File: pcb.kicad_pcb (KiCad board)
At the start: 2 copper layers, 120.7 x 70.6 mm, 11 parts, among them U1 Pico

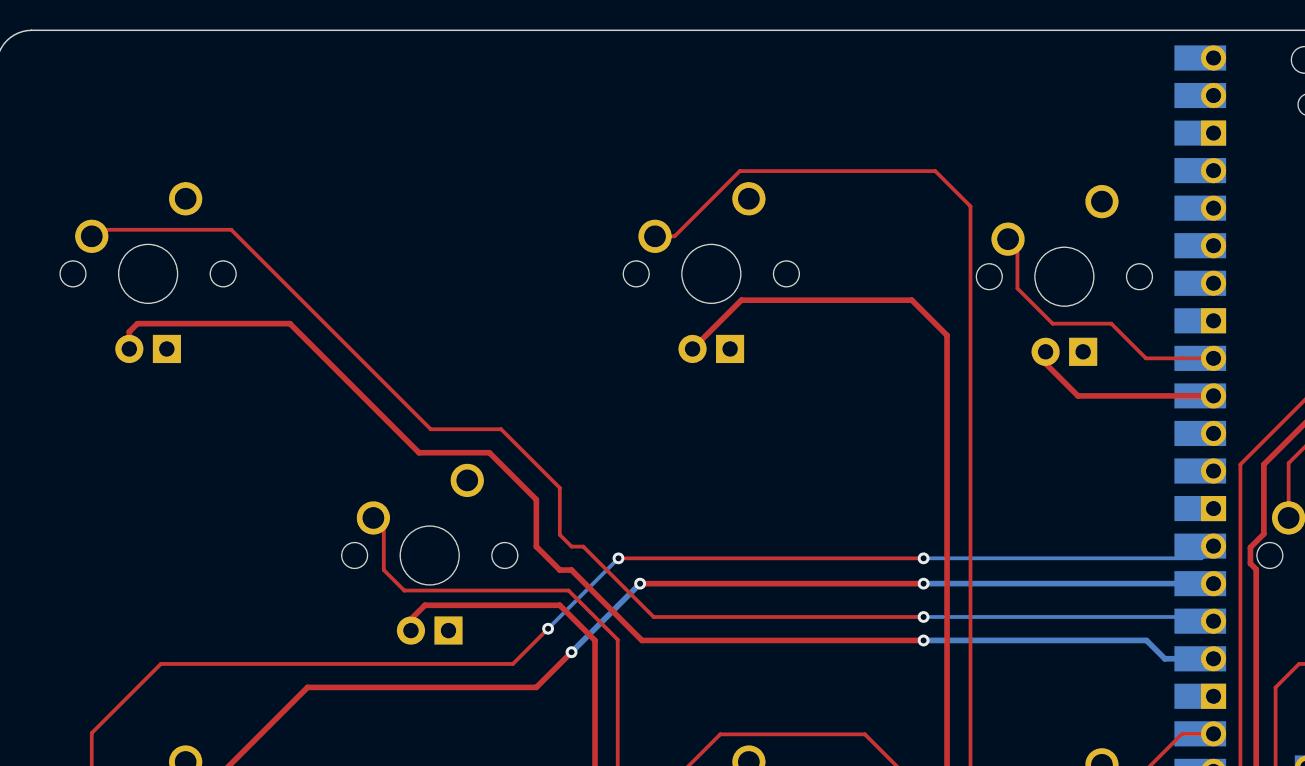
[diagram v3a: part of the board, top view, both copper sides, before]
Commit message: WS2812B strip connector routing
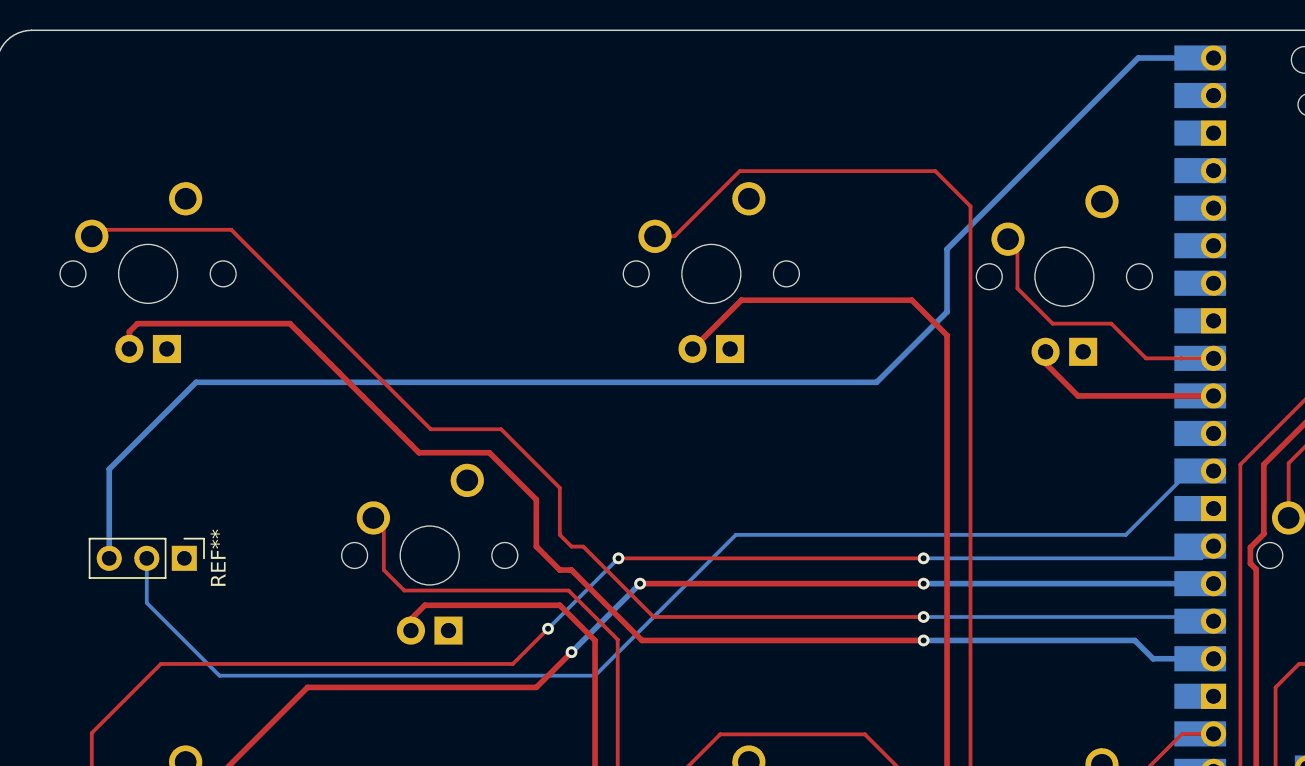
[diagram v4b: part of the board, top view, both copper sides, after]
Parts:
- added REF**: PinHeader_1x03_P2.54mm_Vertical, Connector_PinHeader_2.54mm:PinHeader_1x03_P2.54mm_Vertical, F.Cu at (94.5, 95.2)
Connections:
- U1 pad 29: unconnected-(U1-Pad29) -> DIN
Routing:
- net +5V: track 0.00 -> 94.7 mm
- net DIN: track 0.00 -> 83.0 mm
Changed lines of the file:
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@@
   (net 33 "unconnected-(U1-Pad20)")
   (net 34 "P1 CN")
-  (net 35 "unconnected-(U1-Pad29)")
+  (net 35 "DIN")
   (footprint "MX_Only:MXOnly-1U" (layer "F.Cu")
     (at 192.01775 114.107998)
@@
     (pad "4" thru_hole rect locked (at 1.27 5.08) (size 1.905 1.905) (drill 1.04) (layers *.Cu "B.Mask")
       (net 2 "GND") (pinfunction "LEDGND") (pintype "passive"))
+  )
+  (footprint "Connector_PinHeader_2.54mm:PinHeader_1x03_P2.54mm_Vertical" (layer "F.Cu")
+    (at 94.45625 95.25 -90)
+    (descr "Through hole straight pin header, 1x03, 2.54mm pitch, single row")
+    (tags "Through hole pin header THT 1x03 2.54mm single row")
+    (attr through_hole)
+    (fp_text reference "REF**" (at 0 -2.33 90) (layer "F.SilkS")
+      (effects (font (size 1 1) (thickness 0.15)))
+    )
+    (fp_text value "PinHeader_1x03_P2.54mm_Vertical" (at 0 7.41 90) (layer "F.Fab")
+      (effects (font (size 1 1) (thickness 0.15)))
+    )
+    (fp_text user "${REFERENCE}" (at 0 2.54) (layer "F.Fab")
+      (effects (font (size 1 1) (thickness 0.15)))
+    )
+    (fp_line (start -1.33 6.41) (end 1.33 6.41) (layer "F.SilkS") (width 0.12))
+    (fp_line (start -1.33 1.27) (end -1.33 6.41) (layer "F.SilkS") (width 0.12))
+    (fp_line (start -1.33 -1.33) (end 0 -1.33) (layer "F.SilkS") (width 0.12))
+    (fp_line (start -1.33 1.27) (end 1.33 1.27) (layer "F.SilkS") (width 0.12))
+    (fp_line (start 1.33 1.27) (end 1.33 6.41) (layer "F.SilkS") (width 0.12))
+    (fp_line (start -1.33 0) (end -1.33 -1.33) (layer "F.SilkS") (width 0.12))
+    (fp_line (start 1.8 -1.8) (end -1.8 -1.8) (layer "F.CrtYd") (width 0.05))
+    (fp_line (start -1.8 6.85) (end 1.8 6.85) (layer "F.CrtYd") (width 0.05))
+    (fp_line (start -1.8 -1.8) (end -1.8 6.85) (layer "F.CrtYd") (width 0.05))
+    (fp_line (start 1.8 6.85) (end 1.8 -1.8) (layer "F.CrtYd") (width 0.05))
+    (fp_line (start -1.27 6.35) (end -1.27 -0.635) (layer "F.Fab") (width 0.1))
+    (fp_line (start -0.635 -1.27) (end 1.27 -1.27) (layer "F.Fab") (width 0.1))
+    (fp_line (start -1.27 -0.635) (end -0.635 -1.27) (layer "F.Fab") (width 0.1))
+    (fp_line (start 1.27 -1.27) (end 1.27 6.35) (layer "F.Fab") (width 0.1))
+    (fp_line (start 1.27 6.35) (end -1.27 6.35) (layer "F.Fab") (width 0.1))
+    (pad "1" thru_hole rect (at 0 0 270) (size 1.7 1.7) (drill 1) (layers *.Cu *.Mask)
+      (net 2 "GND"))
+    (pad "2" thru_hole oval (at 0 2.54 270) (size 1.7 1.7) (drill 1) (layers *.Cu *.Mask)
+      (net 35 "DIN"))
+    (pad "3" thru_hole oval (at 0 5.08 270) (size 1.7 1.7) (drill 1) (layers *.Cu *.Mask)
+      (net 1 "+5V"))
+    (model "${KICAD6_3DMODEL_DIR}/Connector_PinHeader_2.54mm.3dshapes/PinHeader_1x03_P2.54mm_Vertical.wrl"
+      (offset (xyz 0 0 0))
+      (scale (xyz 1 1 1))
+      (rotate (xyz 0 0 0))
+    )
   )
   (footprint "MX_Only:MXOnly-1U" (layer "F.Cu")
@@
       (net 2 "GND") (pinfunction "GND") (pintype "power_in"))
     (pad "29" thru_hole oval (at 8.89 -3.81 180) (size 1.7 1.7) (drill 1.02) (layers *.Cu *.Mask)
-      (net 35 "unconnected-(U1-Pad29)") (pinfunction "GPIO22") (pintype "bidirectional"))
+      (net 35 "DIN") (pinfunction "GPIO22") (pintype "bidirectional"))
     (pad "29" smd rect (at 8.89 -3.81 180) (size 3.5 1.7) (drill (offset 0.9 0)) (layers "B.Cu" "B.Mask")
-      (net 35 "unconnected-(U1-Pad29)") (pinfunction "GPIO22") (pintype "bidirectional"))
+      (net 35 "DIN") (pinfunction "GPIO22") (pintype "bidirectional"))
     (pad "30" smd rect (at 8.89 -1.27 180) (size 3.5 1.7) (drill (offset 0.9 0)) (layers "B.Cu" "B.Mask")
       (net 21 "unconnected-(U1-Pad30)") (pinfunction "RUN") (pintype "input"))
@@
   (gr_line (start 202.40625 61.9125) (end 202.40625 127.79375) (layer "Edge.Cuts") (width 0.1))
   (gr_arc (start 202.40625 127.79375) (mid 201.708798 129.477548) (end 200.025 130.175) (layer "Edge.Cuts") (width 0.1))
+  (segment (start 89.37625 89.2175) (end 95.25 83.34375) (width 0.381) (layer "B.Cu") (net 1))
+  (segment (start 158.981632 61.402998) (end 164.07775 61.402998) (width 0.381) (layer "B.Cu") (net 1))
+  (segment (start 95.25 83.34375) (end 141.2875 83.34375) (width 0.381) (layer "B.Cu") (net 1))
+  (segment (start 146.05 78.58125) (end 146.05 74.33463) (width 0.381) (layer "B.Cu") (net 1))
+  (segment (start 141.2875 83.34375) (end 146.05 78.58125) (width 0.381) (layer "B.Cu") (net 1))
+  (segment (start 146.05 74.33463) (end 158.981632 61.402998) (width 0.381) (layer "B.Cu") (net 1))
+  (segment (start 89.37625 95.25) (end 89.37625 89.2175) (width 0.381) (layer "B.Cu") (net 1))
   (segment (start 88.19525 107.06725) (end 88.19525 111.567998) (width 0.254) (layer "F.Cu") (net 3))
   (segment (start 123.825 95.25) (end 144.4625 95.25) (width 0.254) (layer "F.Cu") (net 3))
@@
   (segment (start 110.33125 88.10625) (end 115.09375 88.10625) (width 0.381) (layer "F.Cu") (net 6))
   (via (at 144.4625 100.80625) (size 0.8) (drill 0.4) (layers "F.Cu" "B.Cu") (net 6))
-  (segment (start 159.54375 100.80625) (end 160.780498 102.042998) (width 0.381) (layer "B.Cu") (net 6))
-  (segment (start 160.780498 102.042998) (end 164.07775 102.042998) (width 0.381) (layer "B.Cu") (net 6))
-  (segment (start 144.4625 100.80625) (end 159.54375 100.80625) (width 0.381) (layer "B.Cu") (net 6))
+  (segment (start 159.986748 102.042998) (end 164.07775 102.042998) (width 0.381) (layer "B.Cu") (net 6))
+  (segment (start 158.75 100.80625) (end 159.986748 102.042998) (width 0.381) (layer "B.Cu") (net 6))
+  (segment (start 144.4625 100.80625) (end 158.75 100.80625) (width 0.381) (layer "B.Cu") (net 6))
   (segment (start 109.78525 100.137998) (end 109.78525 99.367875) (width 0.381) (layer "F.Cu") (net 7))
   (segment (start 148.43125 129.38125) (end 162.71875 129.38125) (width 0.381) (layer "F.Cu") (net 7))
@@
   (segment (start 178.59375 98.87309) (end 178.59375 110.33125) (width 0.254) (layer "F.Cu") (net 34))
   (segment (start 171.45 118.26875) (end 161.925 127.79375) (width 0.254) (layer "F.Cu") (net 34))
+  (segment (start 162.46375 89.342998) (end 164.07775 89.342998) (width 0.254) (layer "B.Cu") (net 35))
+  (segment (start 131.7625 93.6625) (end 158.144248 93.6625) (width 0.254) (layer "B.Cu") (net 35))
+  (segment (start 158.144248 93.6625) (end 162.46375 89.342998) (width 0.254) (layer "B.Cu") (net 35))
+  (segment (start 96.8375 103.1875) (end 122.2375 103.1875) (width 0.254) (layer "B.Cu") (net 35))
+  (segment (start 122.2375 103.1875) (end 131.7625 93.6625) (width 0.254) (layer "B.Cu") (net 35))
+  (segment (start 91.91625 98.26625) (end 96.8375 103.1875) (width 0.254) (layer "B.Cu") (net 35))
+  (segment (start 91.91625 95.25) (end 91.91625 98.26625) (width 0.254) (layer "B.Cu") (net 35))
 )

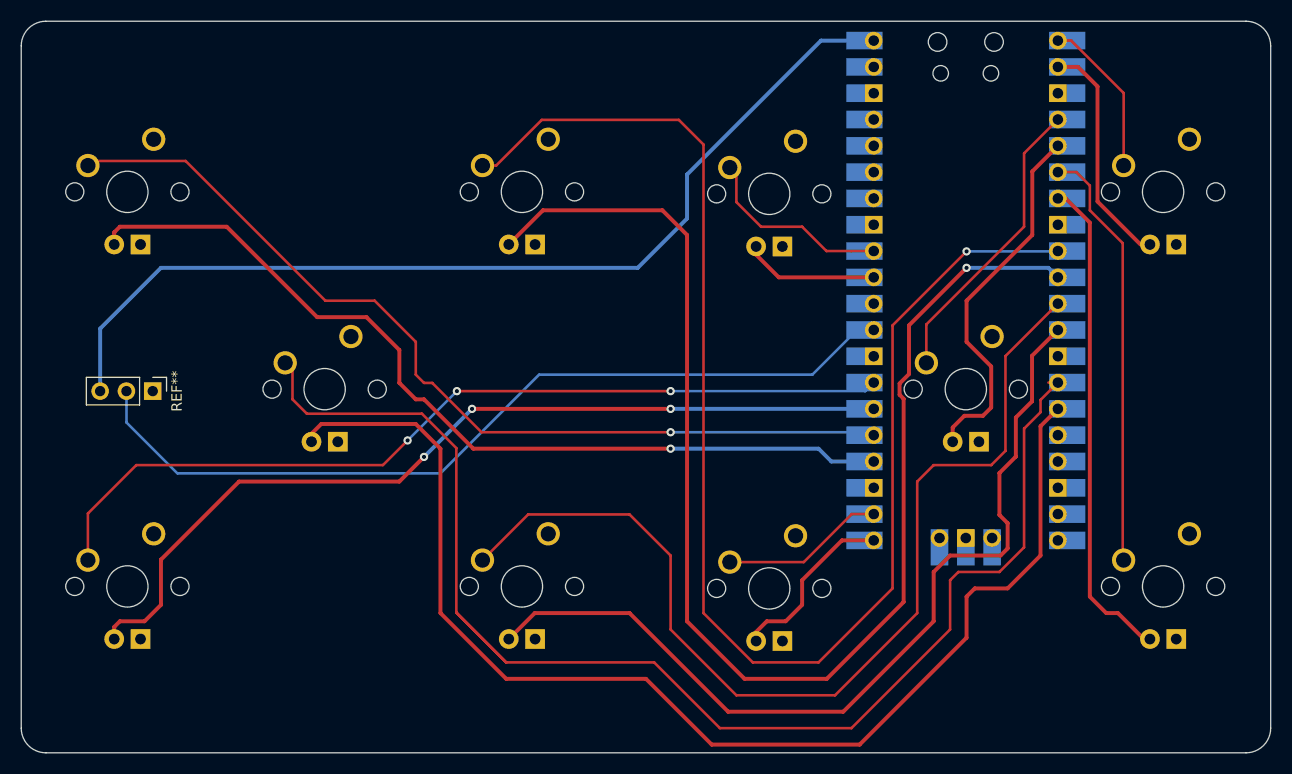
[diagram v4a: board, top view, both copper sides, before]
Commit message: Ground fill
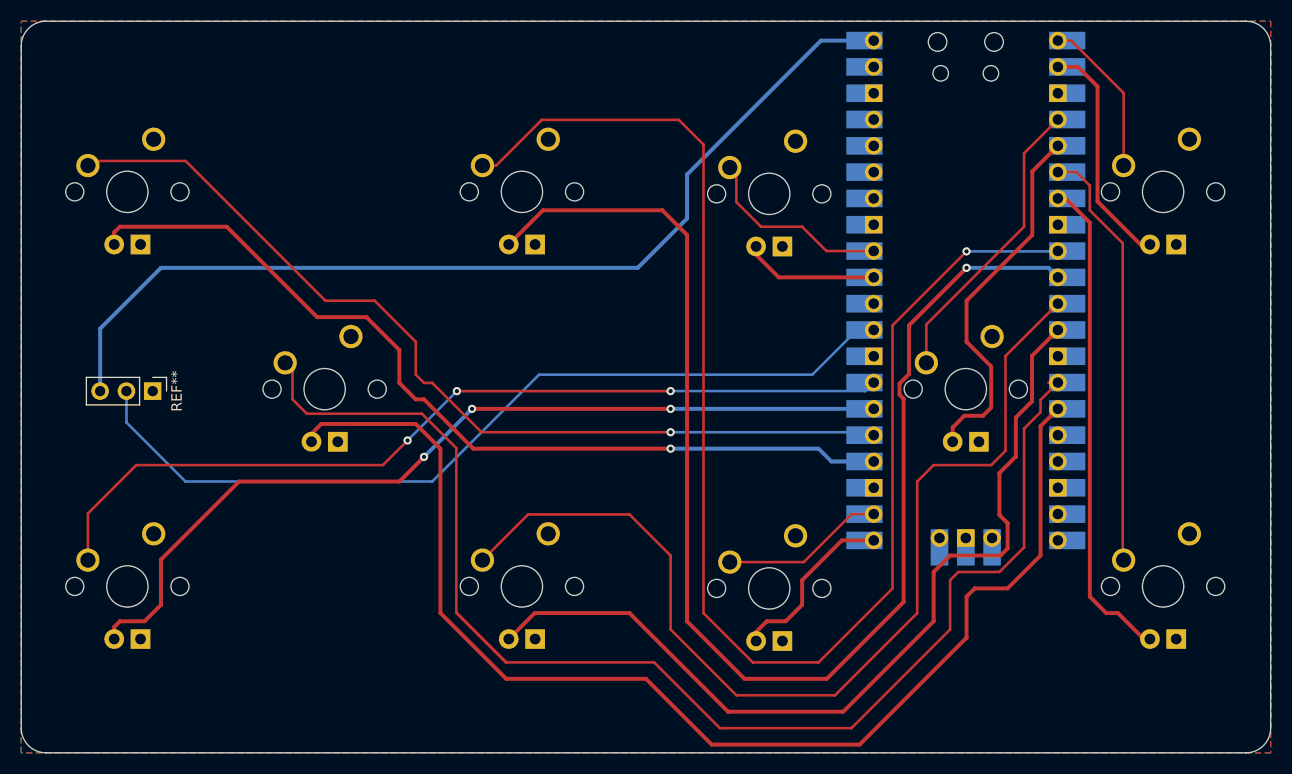
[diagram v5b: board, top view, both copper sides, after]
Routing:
- net DIN: track 83.0 -> 83.6 mm
- added copper zone on B.Cu, net GND
- added copper zone on F.Cu, net GND
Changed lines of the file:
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@@
   (segment (start 178.59375 98.87309) (end 178.59375 110.33125) (width 0.254) (layer "F.Cu") (net 34))
   (segment (start 171.45 118.26875) (end 161.925 127.79375) (width 0.254) (layer "F.Cu") (net 34))
+  (segment (start 121.44375 103.98125) (end 131.7625 93.6625) (width 0.254) (layer "B.Cu") (net 35))
   (segment (start 162.46375 89.342998) (end 164.07775 89.342998) (width 0.254) (layer "B.Cu") (net 35))
   (segment (start 131.7625 93.6625) (end 158.144248 93.6625) (width 0.254) (layer "B.Cu") (net 35))
+  (segment (start 91.91625 98.26625) (end 97.63125 103.98125) (width 0.254) (layer "B.Cu") (net 35))
+  (segment (start 97.63125 103.98125) (end 121.44375 103.98125) (width 0.254) (layer "B.Cu") (net 35))
+  (segment (start 91.91625 95.25) (end 91.91625 98.26625) (width 0.254) (layer "B.Cu") (net 35))
   (segment (start 158.144248 93.6625) (end 162.46375 89.342998) (width 0.254) (layer "B.Cu") (net 35))
-  (segment (start 96.8375 103.1875) (end 122.2375 103.1875) (width 0.254) (layer "B.Cu") (net 35))
-  (segment (start 122.2375 103.1875) (end 131.7625 93.6625) (width 0.254) (layer "B.Cu") (net 35))
-  (segment (start 91.91625 98.26625) (end 96.8375 103.1875) (width 0.254) (layer "B.Cu") (net 35))
-  (segment (start 91.91625 95.25) (end 91.91625 98.26625) (width 0.254) (layer "B.Cu") (net 35))
+  (zone (net 2) (net_name "GND") (layers F&B.Cu) (hatch edge 0.508)
+    (connect_pads (clearance 0.508))
+    (min_thickness 0.254) (filled_areas_thickness no)
+    (fill yes (thermal_gap 0.508) (thermal_bridge_width 0.508))
+    (polygon
+      (pts
+        (xy 202.40625 130.175)
+        (xy 81.75625 130.175)
+        (xy 81.75625 59.53125)
+        (xy 202.40625 59.53125)
+      )
+    )
+  )
 )

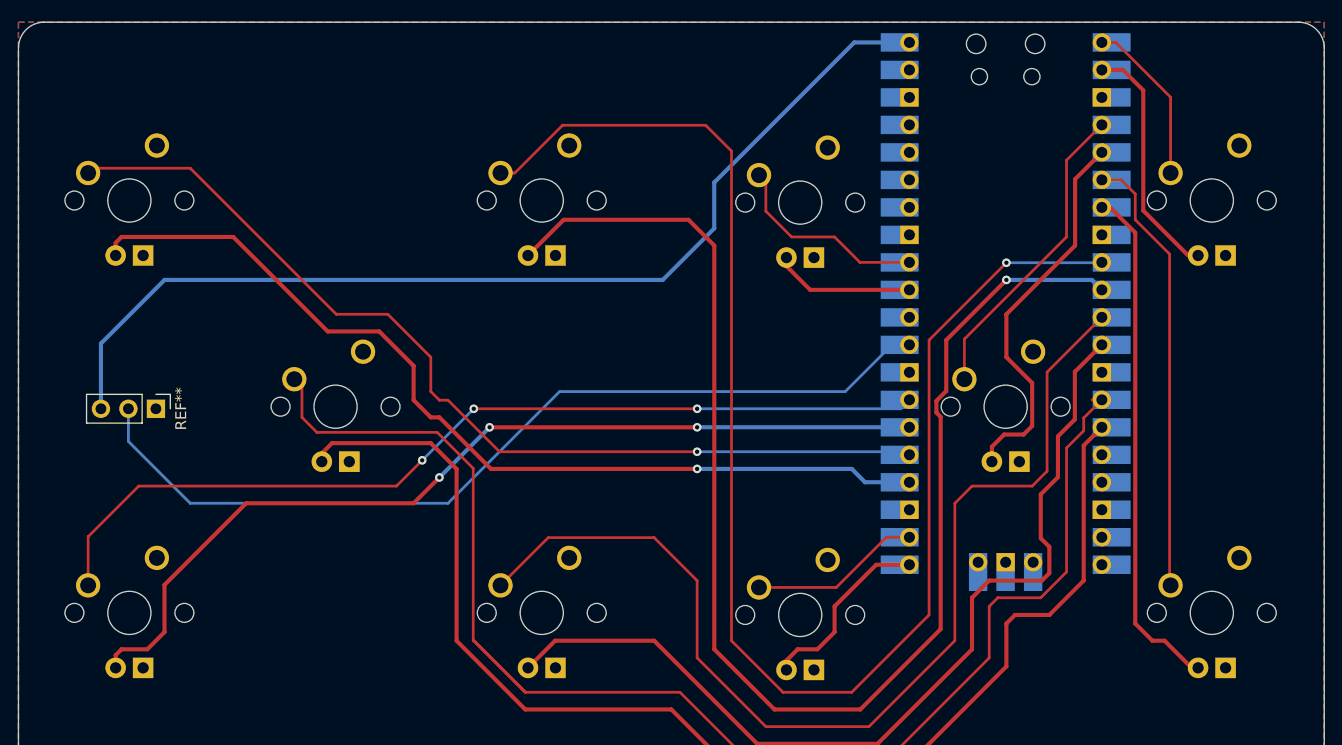
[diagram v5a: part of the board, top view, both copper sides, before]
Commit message: Design rule and minor positioning fixes
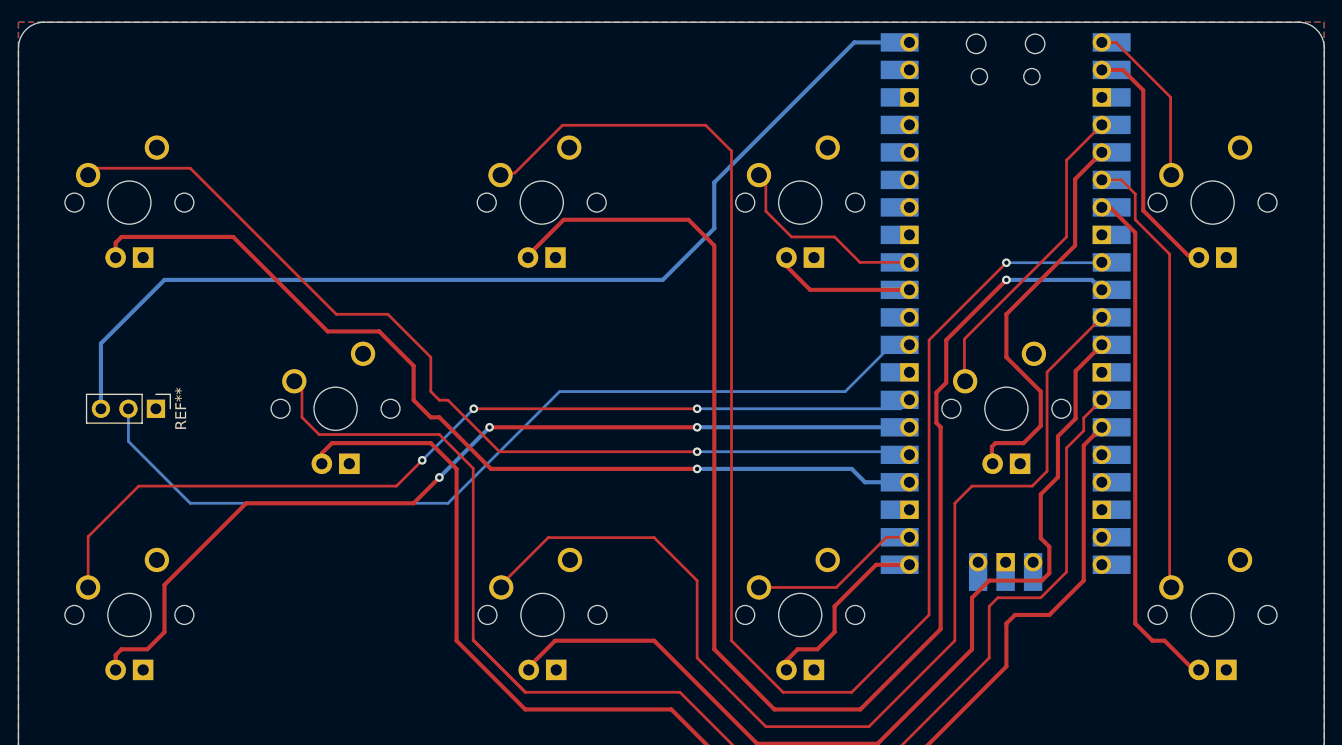
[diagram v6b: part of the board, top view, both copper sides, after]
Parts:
- moved MX10 0.20 mm to (192.1, 114.3)
- moved MX5 0.20 mm to (130.2, 114.3)
- moved MX8 0.20 mm to (173.0, 95.2)
- moved MX9 0.20 mm to (192.1, 76.2)
- moved MX1 0.19 mm to (92.0, 114.3)
- moved MX2 0.19 mm to (92.0, 76.2)
- moved MX3 0.19 mm to (111.1, 95.2)
- moved MX4 0.19 mm to (130.1, 76.2)
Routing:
- net P2 UR: track 17.1 -> 15.4 mm
- net P2 CN LED: track 35.8 -> 36.9 mm
- net P1 CN: track 131.9 -> 131.0 mm
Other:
- board text added: "- +"
- board text added: "HandPump PCB Rev. 1 https://github.com/dj505/handpump"
- board text added: "P1 CN"
- board text added: "P1 DL"
- board text added: "P1 DR"
- board text added: "P1 UL"
- board text added: "P1 UR"
- board text added: "P2 CN"
- board text added: "P2 DL"
- board text added: "P2 UL"
- board text added: "P2 UR"
- board text added: "RPi Pico"
- board text added: "{dblquote}Why settle for 4 when you can have 5?{dblquote}"
